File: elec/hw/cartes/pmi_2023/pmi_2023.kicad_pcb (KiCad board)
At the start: 2 copper layers, 85 x 73 mm, 183 parts, among them J1 USB4105-GF-A-060, J3 con_servo, Q1 2N7002E, SW5 2425755-1, U1 DRV8231ADDAR, U10 AD8531ARTZ, U11 GP2S60B, U12 GP2S60B, U13 GP2S60B, U14 GP2S60B, U15 GP2S60B, U16 GP2S60B, U17 GP2S60B, U18 GP2S60B, U19 tof_sensor_master, U2 SN74LVC1T45DBV, U20 tof_sensor_master, U21 tof_sensor_master, U22 tof_sensor_master, U23 tof_sensor_master, U24 tof_sensor_master, U25 tof_sensor_master, U26 tof_sensor_master, U27 KTS1622EUAA-TR, U28 PCA9685PW, U29 SN74LVC1T45DBV, U3 SN74LVC1T45DBV, U30 SN74LVC1T45DBV, U31 SN74LVC1T45DBV, U32 SN74LVC1T45DBV, U4 DRV8231ADDAR, U5 SN74LVC1T45DBV, U6 SN74LVC1T45DBV, U7 SN74LVC1T45DBV, U8 ESP32-S3-WROOM-1

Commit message: wip
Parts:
- removed C47: 1µF 16V, cocotter_capacitors:C_0805_2012Metric
- removed C48: 10µF 16V, cocotter_capacitors:C_0805_2012Metric
- removed D1: 1SS367,H3F, Diode_SMD:D_SOD-323
- removed D2: green, 0603, cocotter_diodes:LED_0603_1608Metric
- removed D3: yellow, 0603, cocotter_diodes:LED_0603_1608Metric
- removed R10, R11, R9: 0R, cocotter_resistor:r0603_reflow
- removed R12: 100k, cocotter_resistor:r0603_reflow
- removed SERVO0, SERVO1, SERVO2, SERVO3: con_servo, cocotter_connectors:ana_servo_5V
- added BATT_LOW1: red, 0603, cocotter_diodes:LED_0603_1608Metric, F.Cu at (183.8, 109.8)
- added BATT_OK1: red, 0603, cocotter_diodes:LED_0603_1608Metric, F.Cu at (183.8, 116.7)
- added BATT_WARN1: yellow, 0805, cocotter_diodes:LED_0805_2012Metric, F.Cu at (183.5, 113.2)
- added D7: red, 0603, cocotter_diodes:LED_0603_1608Metric, F.Cu at (103.8, 119.2)
- added F1: fuse_holder_5x20mm_TH, cocotter_connectors:PTF-15, F.Cu at (115.3, 104.7)
- added J2: con_servo, cocotter_connectors:ana_servo_5V, F.Cu at (269.4, 51.4)
- added J5: 254, cocotter_connectors:MY-18650-02, F.Cu at (170.6, 91.0)
- added J6: ~, cocotter_connectors:TTL-232R-3V3, F.Cu at (164.0, -77.8)
- added J7: USB4105-GF-A-060, cocotter_connectors:USB4105, F.Cu at (105.5, -81.1)
- added J8: 254, cocotter_connectors:MY-18650-02, F.Cu at (114.4, 91.0)
- added L1: 2.2µH, cocotter_inductors:L_Kyocera_07A7_7.3x6.6mm, F.Cu at (139.0, 20.5)
- added L2: 2.2µH, cocotter_inductors:L_Kyocera_07A7_7.3x6.6mm, F.Cu at (172.5, 103.5)
- added L3: 2.2µH, cocotter_inductors:L_Kyocera_07A7_7.3x6.6mm, F.Cu at (110.5, 113.5)
- added L4: 2.2µH, cocotter_inductors:L_Kyocera_07A7_7.3x6.6mm, F.Cu at (160.8, 103.5)
- added Q2: 2N7002, Package_TO_SOT_SMD:SOT-23, F.Cu at (94.5, -74.8)
- added Q3: DMP2008UFG-7, cocotter_transistors:Diodes_PowerDI3333-8, F.Cu at (118.2, 111.8)
- added R101: 0R, cocotter_resistor:r0603_reflow, F.Cu at (138.1, -45.4)
- added R102: 0R, cocotter_resistor:r0603_reflow, F.Cu at (151.1, -42.9)
- added R103: 0R, cocotter_resistor:r0603_reflow, F.Cu at (111.0, 104.7)
- added R104: 0R, cocotter_resistor:r0603_reflow, F.Cu at (114.0, 104.7)
- added R105: 0R, cocotter_resistor:r0603_reflow, F.Cu at (117.0, 104.7)
- added R106: 0R, cocotter_resistor:r0603_reflow, F.Cu at (119.5, 104.7)
- added R107: 10k, cocotter_resistor:r0603_reflow, F.Cu at (142.5, 29.0)
- added R108: 10k, cocotter_resistor:r0603_reflow, F.Cu at (176.0, 112.0)
- added R109: 100k, cocotter_resistor:r0603_reflow, F.Cu at (245.0, 97.0)
- added R110: 90k, cocotter_resistor:r0603_reflow, F.Cu at (113.0, 119.8)
- added R111: 10k, cocotter_resistor:r0603_reflow, F.Cu at (114.0, 122.0)
- added R112: 90k, cocotter_resistor:r0603_reflow, F.Cu at (164.0, 109.2)
- added R113: 10k, cocotter_resistor:r0603_reflow, F.Cu at (163.2, 111.5)
- added R114: 1k 1%, cocotter_resistor:r0603_reflow, F.Cu at (106.5, 118.5)
- added R13: 1k 1%, cocotter_resistor:r0603_reflow, F.Cu at (167.2, 129.8)
- added R20: 1k 1%, cocotter_resistor:r0603_reflow, F.Cu at (127.5, 132.5)
- added R21: 1k 1%, cocotter_resistor:r0603_reflow, F.Cu at (130.2, 134.0)
- added R22: 1k 1%, cocotter_resistor:r0603_reflow, F.Cu at (157.5, 134.0)
- added R25: 1k 1%, cocotter_resistor:r0603_reflow, F.Cu at (157.5, 132.5)
- added R26: 1k 1%, cocotter_resistor:r0603_reflow, F.Cu at (127.5, 135.5)
- added R57: 0R, cocotter_resistor:r0603_reflow, F.Cu at (168.0, 122.2)
- added R58: 0R, cocotter_resistor:r0603_reflow, F.Cu at (168.0, 119.2)
- added R59: 0R, cocotter_resistor:r0603_reflow, F.Cu at (171.2, 122.0)
- added R60: 0R, cocotter_resistor:r0603_reflow, F.Cu at (172.8, 122.0)
- added R61: 0R, cocotter_resistor:r0603_reflow, F.Cu at (168.0, 117.8)
- added R62: 1k 1%, cocotter_resistor:r0603_reflow, F.Cu at (182.2, 116.5)
- added R63: 1k 1%, cocotter_resistor:r0603_reflow, F.Cu at (181.8, 113.0)
- added SW6: 2425755-1, cocotter_connectors:2425755-1, F.Cu at (123.7, -49.4)
- added SW7: MSS12C02LS-BB2.0, cocotter_connectors:MSS12C02LS-BB2.0, F.Cu at (95.2, -78.0)
- added SW8: MSS12C02LS-BB2.0, cocotter_connectors:MSS12C02LS-BB2.0, F.Cu at (104.2, 114.0)
- added TP1: TestPoint, cocotter_others:testpoint-THT-0.5mm, F.Cu at (123.5, 114.5)
- added TP2: TestPoint, cocotter_others:testpoint-THT-0.5mm, F.Cu at (123.5, 116.2)
- added TP3: TestPoint, cocotter_others:testpoint-THT-0.5mm, F.Cu at (146.0, 140.5)
- added TP4: TestPoint, cocotter_others:testpoint-THT-0.5mm, F.Cu at (146.0, 142.0)
- added TP5: TestPoint, cocotter_others:testpoint-THT-0.5mm, F.Cu at (139.0, 139.0)
- added TP6: TestPoint, cocotter_others:testpoint-THT-0.5mm, F.Cu at (139.0, 137.5)
- added TP7: TestPoint, cocotter_others:testpoint-THT-0.5mm, F.Cu at (135.9, -48.2)
- added TP8: TestPoint, cocotter_others:testpoint-THT-0.5mm, F.Cu at (180.5, 123.5)
- added U34: TLV61070A, cocotter_ic:SOT-23-6, F.Cu at (161.0, 109.0)
- added U35: LDL1117S33R, cocotter_ic:SOT-223, F.Cu at (150.0, 23.2)
- C10, C31, C9: moved to B.Cu
- C11: value 22µF 16V -> 10µF 25V; footprint cocotter_capacitors:C_1206_3216Metric -> cocotter_capacitors:C_0805_2012Metric; moved to B.Cu
- C12, C3, C4: value 22µF 16V -> 100nF 50V; footprint cocotter_capacitors:C_1206_3216Metric -> cocotter_capacitors:C_0603_1608Metric
- C14, C23, C24, C26, C35: value 100nF 50V -> 10µF 25V; footprint cocotter_capacitors:C_0603_1608Metric -> cocotter_capacitors:C_0805_2012Metric
- C20, C28: value 10µF 16V -> 100nF 50V; footprint cocotter_capacitors:C_0805_2012Metric -> cocotter_capacitors:C_0603_1608Metric
- C25, C46: value 10µF 16V -> 10µF 25V
- C27, C30, C39, C40: value 100nF 50V -> 10µF 16V; footprint cocotter_capacitors:C_0603_1608Metric -> cocotter_capacitors:C_0805_2012Metric
- C29, C37, C41: value 100nF 50V -> 18nF 50V
- C36, C38, C5, C6: value 100nF 50V -> 47µF 10V; footprint cocotter_capacitors:C_0603_1608Metric -> cocotter_capacitors:C_1206_3216Metric
- C42: value 10µF 16V -> 18nF 50V; footprint cocotter_capacitors:C_0805_2012Metric -> cocotter_capacitors:C_0603_1608Metric
- C43, C44: value 10µF 16V -> 47µF 10V; footprint cocotter_capacitors:C_0805_2012Metric -> cocotter_capacitors:C_1206_3216Metric
- C45: value 10µF 16V -> 1µF 50V
- D5: value green, 0603 -> red, 0603
- D6: value green, 0603 -> 1N5819WS; footprint cocotter_diodes:LED_0603_1608Metric -> cocotter_diodes:D_SOD-323F
- J1: value USB4105-GF-A-060 -> con_servo; footprint cocotter_connectors:USB4105 -> cocotter_connectors:ana_servo_5V
- J4: value ~ -> con_servo; footprint cocotter_connectors:1051 -> cocotter_connectors:ana_servo_5V
- Q1: value 2N7002E -> ~; footprint Package_TO_SOT_SMD:SOT-23 -> cocotter_transistors:SOT-23-3
- R14, R15, R19, R23, R24, R27, R28, R64, R82, R83, R97, R98, R99: value 100k -> 1k 1%
- R16, R17, R18: value 10k -> 1k 1%
- R29, R54, R55, R56, R8: value 100k -> 0R
- R3, R38, R4, R5: value 10k -> 100k
- R31: value 0R -> 100k; moved to B.Cu
- R32, R87, R88, R89, R90, R93: value 0R -> 100k
- R34, R35, R46: value 100k -> 150R 1%; footprint cocotter_resistor:r0603_reflow -> cocotter_resistor:r0805_reflow; moved to B.Cu
- R36: value 0R -> 27k 1%; moved to B.Cu
- R37, R42, R43, R52, R53: value 100k -> 27k 1%; moved to B.Cu
- R40, R41, R47, R50, R51: value 1k 1% -> 150R 1%; footprint cocotter_resistor:r0603_reflow -> cocotter_resistor:r0805_reflow; moved to B.Cu
- R48, R49: value 1k 1% -> 27k 1%; moved to B.Cu
- R6, R7: value 0R -> 3k3 1%
- R65, R75: value 150R 1% -> 0R; footprint cocotter_resistor:r0805_reflow -> cocotter_resistor:r0603_reflow; moved to F.Cu
- R66: value 27k 1% -> 68k 1%; moved to F.Cu
- R67: value 150R 1% -> 90k; footprint cocotter_resistor:r0805_reflow -> cocotter_resistor:r0603_reflow; moved to F.Cu
- R68, R70: value 27k 1% -> 100k
- R69, R71: value 150R 1% -> 100k; footprint cocotter_resistor:r0805_reflow -> cocotter_resistor:r0603_reflow
- R72, R74, R76, R78: value 27k 1% -> 100k; moved to F.Cu
- R73, R77, R79: value 150R 1% -> 100k; footprint cocotter_resistor:r0805_reflow -> cocotter_resistor:r0603_reflow; moved to F.Cu
- R80: value 27k 1% -> 1k 1%
- R81: value 100k -> 1k 1%; moved to B.Cu
- R91, R92: value 0R -> 1k 1%
- R94: value 0R -> 10k
- R96: value 1k 1% -> 100k
- SW5: value 2425755-1 -> DS1040-04RN; footprint cocotter_connectors:2425755-1 -> cocotter_connectors:DS1040-04RN
- U10: value AD8531ARTZ -> tof_sensor_master; footprint cocotter_ic:SOT23-5 -> cocotter_connectors:tof_sensor_male
- U11, U17, U18: value GP2S60B -> tof_sensor_master; footprint cocotter_ic:GP2S60 -> cocotter_connectors:tof_sensor_male; moved to F.Cu
- U12: value GP2S60B -> LSM6DSO32XTR; footprint cocotter_ic:GP2S60 -> cocotter_ic:LGA-14_3x2.5mm_P0.5mm_LayoutBorder3x4y; moved to F.Cu
- U19, U20: value tof_sensor_master -> GP2S60B; footprint cocotter_connectors:tof_sensor_male -> cocotter_ic:GP2S60; moved to B.Cu
- U2: value SN74LVC1T45DBV -> DRV8231ADDAR; footprint Package_TO_SOT_SMD:SOT-23-6 -> cocotter_ic:DDA0008B
- U23: value tof_sensor_master -> PCA9685PW; footprint cocotter_connectors:tof_sensor_male -> Package_SO:TSSOP-28_4.4x9.7mm_P0.65mm
- U24, U25, U26: value tof_sensor_master -> SN74LVC1T45DBV; footprint cocotter_connectors:tof_sensor_male -> Package_TO_SOT_SMD:SOT-23-6
- U27: value KTS1622EUAA-TR -> SN74LVC1T45DBV; footprint cocotter_ic:TQFN44-24 -> Package_TO_SOT_SMD:SOT-23-6
- U28: value PCA9685PW -> TLV61070A; footprint Package_SO:TSSOP-28_4.4x9.7mm_P0.65mm -> cocotter_ic:SOT-23-6
- U29: value SN74LVC1T45DBV -> TLV61070A; footprint Package_TO_SOT_SMD:SOT-23-6 -> cocotter_ic:SOT-23-6
- U3: value SN74LVC1T45DBV -> EESX1321; footprint Package_TO_SOT_SMD:SOT-23-6 -> cocotter_ic:EESX1321
- U30: value SN74LVC1T45DBV -> TCA9535PWR; footprint Package_TO_SOT_SMD:SOT-23-6 -> Package_SO:TSSOP-24_4.4x7.8mm_P0.65mm
- U31: value SN74LVC1T45DBV -> ~; footprint Package_TO_SOT_SMD:SOT-23-6 -> cocotter_ic:OLED_0.96inch
- U32: value SN74LVC1T45DBV -> ESP32-S3-WROOM-1; footprint Package_TO_SOT_SMD:SOT-23-6 -> cocotter_ic:ESP32-S3-WROOM-1
- U33: value ~ -> TLV61070A; footprint cocotter_ic:OLED_0.96inch -> cocotter_ic:SOT-23-6
- U4: value DRV8231ADDAR -> EESX1321; footprint cocotter_ic:DDA0008B -> cocotter_ic:EESX1321
- U5: value SN74LVC1T45DBV -> AD8531ARTZ; footprint Package_TO_SOT_SMD:SOT-23-6 -> cocotter_ic:SOT23-5; moved to B.Cu
- U6, U7: value SN74LVC1T45DBV -> tof_sensor_master; footprint Package_TO_SOT_SMD:SOT-23-6 -> cocotter_connectors:tof_sensor_male
- U8: value ESP32-S3-WROOM-1 -> GP2S60B; footprint cocotter_ic:ESP32-S3-WROOM-1 -> cocotter_ic:GP2S60; moved to B.Cu
- U9: value ~ -> GP2S60B; footprint cocotter_ic:LGA-14_3x2.5mm_P0.5mm_LayoutBorder3x4y -> cocotter_ic:GP2S60; moved to B.Cu
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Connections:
- C10 pad 1: +BATT -> +3.3V
- C11 pad 1: +BATT -> +3.3V
- C12 pad 1: +BATT -> +3.3V
- C13 pad 1: /propulsion/encoder_supply -> +3V3
- C14 pad 1: /propulsion/encoder_supply -> +3V3
- C15 pad 1: +3.3V -> +3V3
- C16 pad 1: +3.3V -> +3V3
- C17 pad 1: +3.3V -> +3V3
- C18 pad 1: Net-(J3-5V) -> +3V3
- C19 pad 1: /com/EN_ESP32_3v3 -> +5V
- C2 pad 1: +BATT -> +3.3V
- C20 pad 1: +3.3V -> +5V
- C21 pad 1: +3.3V -> +5V
- C22 pad 1: /com/esp32_vbatt_mon_2v9 -> +5V
- C23 pad 1: +3.3V -> +5V
- C24 pad 1: Net-(U10-+) -> +5V
- C25 pad 1: +3.3V -> +5V
- C26 pad 1: +3.3V -> +5V
- C27 pad 1: +3V3 -> +BATT
- C29 pad 1: +3V3 -> /power_supply/P3V9
- C29 pad 2: GND -> Net-(U28-FB)
- C3 pad 1: +BATT -> /propulsion/Vmot_left_5V
- C30 pad 1: +5V -> +BATT
- C31 pad 1: +3V3 -> +3.3V
- C32 pad 1: +5V -> /com/EN_ESP32_3v3
- C33 pad 1: +3V3 -> /com/esp32_vbatt_mon_2v9
- C34 pad 1: +5V -> +3.3V
- C35 pad 1: +3V3 -> +3.3V
- C36 pad 1: +5V -> /power_supply/P3V9
- C37 pad 1: +3V3 -> +5V
- C37 pad 2: GND -> Net-(U29-FB)
- C39 pad 1: +3.3V -> +BATT
- C4 pad 1: +BATT -> /propulsion/Vmot_right_5V
- C40 pad 1: /propulsion/encoder_supply -> +BATT
- C41 pad 1: /propulsion/encoder_supply -> /power_supply/Vmot_left_5V
- C41 pad 2: GND -> Net-(U33-FB)
- C42 pad 1: +5V -> /power_supply/Vmot_right_5V
- C42 pad 2: GND -> Net-(U34-FB)
- C43 pad 1: Net-(J3-5V) -> /power_supply/Vmot_left_5V
- C44 pad 1: +5V -> /power_supply/Vmot_right_5V
- C45 pad 1: +5V -> /power_supply/P3V9
- C46 pad 1: +5V -> +3.3V
- C5 pad 1: +3.3V -> /propulsion/Vmot_left_5V
- C6 pad 1: /propulsion/encoder_supply -> /propulsion/Vmot_right_5V
- C8 pad 1: +3.3V -> /propulsion/encoder_supply
- C9 pad 1: +3.3V -> Net-(U5-+)
- D4 pad A: (no net) -> Net-(D4-PadA)
- D4 pad C: (no net) -> GND
- D5 pad A: (no net) -> Net-(D5-PadA)
- D5 pad C: (no net) -> GND
- J3 pad 2: Net-(J3-5V) -> +5V
- J3 pad 3: /propulsion/pwm_vaccum_5v -> /actuators/servo_pwm_2_5V
- Q1 pad 1: /com/USB_VBUS -> /propulsion/pwm_vaccum_3v3
- R1 pad 1: /propulsion/pwm_left -> /propulsion/dir_left
- R100 pad 1: +3.3V -> Net-(R100-Pad1)
- R100 pad 2: /interface/esp32_sda_3v3 -> /com/scl_3v3
- R14 pad 1: /propulsion/dir_right -> Net-(U3-C2)
- R15 pad 1: /propulsion/pwm_right -> Net-(U4-C1)
- R16 pad 1: /com/i_prop_right_3v3 -> Net-(U4-C2)
- R17 pad 1: /com/i_prop_right_3v3 -> Net-(U3-E2)
- R17 pad 2: GND -> /propulsion/right_encod_B_3v3
- R18 pad 1: /com/i_prop_right_3v3 -> /propulsion/right_encod_B_3v3
- R19 pad 1: +3.3V -> Net-(U3-E2)
- R19 pad 2: /propulsion/nREAD_encoder_3v3 -> /propulsion/right_encod_B_3v3
- R2 pad 1: /propulsion/dir_left -> /propulsion/dir_right
- R23 pad 1: /propulsion/right_encod_A_5V -> /propulsion/right_encod_A_3v3
- R24 pad 1: /propulsion/right_encod_B_5V -> Net-(U4-E2)
- R24 pad 2: GND -> /propulsion/left_encod_B_3v3
- R27 pad 1: +3.3V -> /propulsion/left_encod_A_3v3
- R27 pad 2: /com/EN_ESP32_3v3 -> GND
- R28 pad 1: Net-(U8-IO46,GPIO46) -> Net-(U4-E1)
- R28 pad 2: GND -> /propulsion/left_encod_A_3v3
- R29 pad 1: /propulsion/pwm_vaccum_3v3 -> /propulsion/encoder_supply
- R29 pad 2: GND -> +5V
- R3 pad 1: /com/i_prop_left_3v3 -> /propulsion/pwm_left
- R30 pad 1: Net-(U7-DIR) -> /propulsion/encoder_supply
- R31 pad 1: Net-(J3-5V) -> /actuators/line_led_pwm_3v3
- R31 pad 2: +5V -> Net-(U5-+)
- R32 pad 1: Net-(J3-5V) -> +3.3V
- R32 pad 2: +3.3V -> /sensors/ctc_left
- R33 pad 2: Net-(U8-IO45,GPIO45) -> /sensors/ctc_rigth
- R34 pad 1: Net-(U8-IO45,GPIO45) -> /sensors/line_led_3v3
- R34 pad 2: GND -> Net-(U8-A)
- R35 pad 1: +3V3 -> /sensors/line_led_3v3
- R35 pad 2: /com/i2C_io_int_3v3 -> Net-(U9-A)
- R36 pad 1: Net-(U27-ADDR) -> +3.3V
- R36 pad 2: GND -> /line_detect_l0
- R37 pad 1: +3V3 -> +3.3V
- R37 pad 2: Net-(U27-nRESET) -> /line_detect_r0
- R38 pad 1: /com/boot/dl_select_3v3 -> +3.3V
- R38 pad 2: Net-(R38-Pad2) -> Net-(U12-INT2/DEN)
- R39 pad 2: /com/boot/dl_select_3v3 -> /com/gyro_ncs_3v3
- R4 pad 1: /com/i_prop_left_3v3 -> /propulsion/pwm_right
- R40 pad 1: Net-(U8-TXD0,U0TXD,GPIO43,CLK_OUT1) -> /sensors/line_led_3v3
- R40 pad 2: /com/esp32_dbg_tx_3v3 -> Net-(U13-A)
- R41 pad 1: Net-(U8-TXD0,U0TXD,GPIO43,CLK_OUT1) -> /sensors/line_led_3v3
- R41 pad 2: /com/esp32_dbg_tx_3v3 -> Net-(U14-A)
- R42 pad 1: /interface/conf0 -> +3.3V
- R42 pad 2: GND -> /line_detect_l1
- R43 pad 2: /com/esp32_dbg_rx_3v3 -> /line_detect_r1
- R44 pad 1: Net-(R44-Pad1) -> +3.3V
- R44 pad 2: /com/vbatt_mon_8.7V -> Net-(U12-SCx)
- R45 pad 1: /com/esp32_vbatt_mon_2v9 -> +3.3V
- R45 pad 2: Net-(R44-Pad1) -> Net-(U12-SDx)
- R46 pad 1: GND -> /sensors/line_led_3v3
- R46 pad 2: /com/esp32_vbatt_mon_2v9 -> Net-(U15-A)
- R47 pad 1: /com/led_esp_3v3 -> /sensors/line_led_3v3
- R47 pad 2: Net-(D5-A) -> Net-(U16-A)
- R48 pad 1: /com/led_com_3v3 -> +3.3V
- R48 pad 2: Net-(D6-A) -> /line_detect_l2
- R49 pad 1: +3V3 -> +3.3V
- R49 pad 2: Net-(D2-A) -> /line_detect_r2
- R5 pad 1: /com/i_prop_left_3v3 -> /propulsion/pwm_vaccum_3v3
- R50 pad 1: +3V3 -> /sensors/line_led_3v3
- R50 pad 2: Net-(D3-A) -> Net-(U19-A)
- R51 pad 1: +3V3 -> /sensors/line_led_3v3
- R51 pad 2: Net-(D4-A) -> Net-(U20-A)
- R52 pad 1: /com/USB_VBUS -> +3.3V
- R52 pad 2: GND -> /line_detect_l3
- R53 pad 2: Net-(U9-SCx) -> /line_detect_r3
- R54 pad 1: +3.3V -> Net-(U23-EXTCLK)
- R54 pad 2: Net-(U9-SDx) -> GND
- R55 pad 1: +3.3V -> /actuators/servos_nOE
- R55 pad 2: /com/gyro_ncs_3v3 -> GND
- R56 pad 1: +3.3V -> Net-(U23-A1)
- R56 pad 2: Net-(U9-INT1) -> GND
- R6 pad 1: +5V -> /com/i_prop_right_3v3
- R6 pad 2: /propulsion/encoder_supply -> GND
- R64 pad 1: /actuators/line_led_pwm_3v3 -> +3V3
- R64 pad 2: Net-(U10-+) -> Net-(BATT_LOW1-PadA)
- R65 pad 1: /sensors/line_led_3v3 -> +BATT
- R65 pad 2: Net-(U11-A) -> /com/vbatt_mon_4.35V
- R66 pad 1: +3.3V -> /power_supply/P3V9
- R66 pad 2: /line_detect_l0 -> Net-(U28-FB)
- R67 pad 1: /sensors/line_led_3v3 -> +5V
- R67 pad 2: Net-(U12-A) -> Net-(U29-FB)
- R68 pad 1: +3.3V -> /interface/conf0
- R68 pad 2: /line_detect_l1 -> GND
- R69 pad 1: /sensors/line_led_3v3 -> /interface/conf1
- R69 pad 2: Net-(U13-A) -> GND
- R7 pad 1: +3.3V -> /com/i_prop_left_3v3
- R7 pad 2: /propulsion/encoder_supply -> GND
- R70 pad 1: +3.3V -> /interface/conf2
- R70 pad 2: /line_detect_l2 -> GND
- R71 pad 1: /sensors/line_led_3v3 -> /interface/conf3
- R71 pad 2: Net-(U14-A) -> GND
- R72 pad 1: +3.3V -> /interface/select2
- R72 pad 2: /line_detect_l3 -> GND
- R73 pad 1: /sensors/line_led_3v3 -> /interface/select1
- R73 pad 2: Net-(U15-A) -> GND
- R74 pad 1: +3.3V -> +3V3
- R74 pad 2: /line_detect_r0 -> /com/i2C_io_int_3v3
- R75 pad 1: /sensors/line_led_3v3 -> Net-(U30-A2)
- R75 pad 2: Net-(U16-A) -> GND
- R76 pad 1: +3.3V -> +3V3
- R76 pad 2: /line_detect_r1 -> /interface/u30_unused_p17
- R77 pad 1: /sensors/line_led_3v3 -> /interface/select4
- R77 pad 2: Net-(U17-A) -> GND
- R78 pad 1: +3.3V -> /interface/select3
- R78 pad 2: /line_detect_r2 -> GND
- R79 pad 1: /sensors/line_led_3v3 -> /interface/select0
- R79 pad 2: Net-(U18-A) -> GND
- R8 pad 1: /propulsion/left_encod_A_5V -> Net-(R8-Pad1)
- R8 pad 2: GND -> /propulsion/Vmot_left_5V
- R80 pad 2: /line_detect_r3 -> /interface/esp32_scl_3v3
- R81 pad 2: /sensors/ctc_left -> /interface/esp32_sda_3v3
- R82 pad 1: +3.3V -> /com/led_esp_3v3
- R82 pad 2: /sensors/ctc_rigth -> Net-(D4-PadA)
- R83 pad 1: /interface/conf1 -> /com/led_com_3v3
- R83 pad 2: GND -> Net-(D5-PadA)
- R84 pad 1: /interface/conf2 -> GND
- R84 pad 2: GND -> /com/esp32_vbatt_mon_2v9
- R85 pad 1: /interface/conf3 -> /com/esp32_vbatt_mon_2v9
- R85 pad 2: GND -> /com/vbatt_mon_4.35V
- R86 pad 1: /interface/select2 -> +3.3V
- R86 pad 2: GND -> /com/EN_ESP32_3v3
- R87 pad 1: /actuators/servos_nOE -> /com/esp32_vbatt_mon_2v9
- R87 pad 2: GND -> /com/vbatt_mon_4.35V
- R88 pad 1: Net-(U28-EXTCLK) -> +3.3V
- R88 pad 2: GND -> Net-(U32-IO45,GPIO45)
- R89 pad 1: Net-(U28-A1) -> Net-(U32-IO45,GPIO45)
- R90 pad 1: Net-(U28-A2) -> Net-(U32-IO46,GPIO46)
- R91 pad 1: Net-(U28-A4) -> Net-(U32-TXD0,U0TXD,GPIO43,CLK_OUT1)
- R91 pad 2: GND -> /com/esp32_dbg_tx_3v3
- R92 pad 1: +3V3 -> Net-(U32-TXD0,U0TXD,GPIO43,CLK_OUT1)
- R92 pad 2: Net-(U28-A0) -> /com/esp32_dbg_tx_3v3
- R93 pad 1: +3V3 -> +3.3V
- R93 pad 2: Net-(U28-A3) -> /com/boot/dl_select_3v3
- R94 pad 1: +3V3 -> /com/boot/dl_select_3v3
- R94 pad 2: Net-(U28-A5) -> Net-(R94-Pad2)
- R95 pad 1: /interface/select1 -> +3.3V
- R95 pad 2: GND -> /com/esp32_dbg_rx_3v3
- R96 pad 1: +3.3V -> /com/USB_VBUS
- R96 pad 2: /interface/esp32_scl_3v3 -> GND
- R97 pad 1: /interface/select4 -> Net-(R97-Pad1)
- R97 pad 2: GND -> /com/sda_3v3
- R98 pad 1: /interface/select3 -> +3.3V
- R98 pad 2: GND -> Net-(R97-Pad1)
- R99 pad 1: /interface/select0 -> +3.3V
- R99 pad 2: GND -> Net-(R100-Pad1)
- SW5 pad 1: /interface/select0 -> /interface/conf0
- SW5 pad 2: /interface/select4 -> /interface/conf1
- SW5 pad 3: /interface/select3 -> /interface/conf2
- SW5 pad 4: /interface/select2 -> /interface/conf3
- SW5 pad 6: /interface/select1 -> +3.3V
- U1 pad 5: +BATT -> /propulsion/Vmot_left_5V
- U1 pad 6: Net-(ML1-M+) -> /propulsion/mot_left_A
- U1 pad 8: Net-(ML1-M-) -> /propulsion/mot_left_B
- U10 pad 1: /sensors/line_led_3v3 -> GND
- U10 pad 2: GND -> +3.3V
- U10 pad 3: Net-(U10-+) -> /sensors/enable_tof2
- U10 pad 4: /sensors/line_led_3v3 -> /sensors/tof_irq
- U10 pad 5: +3.3V -> /com/sda_3v3
- U11 pad 1: /line_detect_l0 -> GND
- U11 pad 2: GND -> +3.3V
- U11 pad 3: GND -> /sensors/enable_tof6
- U11 pad 4: Net-(U11-A) -> /sensors/tof_irq
- U12 pad 1: /line_detect_l1 -> /com/gyro_miso_3v3
- U12 pad 2: GND -> Net-(U12-SDx)
- U12 pad 3: GND -> Net-(U12-SCx)
- U12 pad 4: Net-(U12-A) -> Net-(U12-INT1)
- U13 pad 1: /line_detect_l2 -> /line_detect_l1
- U14 pad 1: /line_detect_l3 -> /line_detect_r1
- U15 pad 1: /line_detect_r0 -> /line_detect_l2
- U16 pad 1: /line_detect_r1 -> /line_detect_r2
- U17 pad 1: /line_detect_r2 -> GND
- U17 pad 2: GND -> +3.3V
- U17 pad 3: GND -> /sensors/enable_tof3
- U17 pad 4: Net-(U17-A) -> /sensors/tof_irq
- U18 pad 1: /line_detect_r3 -> GND
- U18 pad 2: GND -> +3.3V
- U18 pad 3: GND -> /sensors/enable_tof7
- U18 pad 4: Net-(U18-A) -> /sensors/tof_irq
- U19 pad 1: GND -> /line_detect_l3
- U19 pad 2: +3.3V -> GND
- U19 pad 3: /sensors/enable_tof1 -> GND
- U19 pad 4: /sensors/tof_irq -> Net-(U19-A)
- U2 pad 1: +3.3V -> /com/i_prop_right_3v3
- U2 pad 2: GND -> /propulsion/dir_right
- U2 pad 3: /propulsion/left_encod_A_3v3 -> /propulsion/pwm_right
- U2 pad 4: /propulsion/left_encod_A_5V -> +3.3V
- U2 pad 5: /propulsion/nREAD_encoder_3v3 -> /propulsion/Vmot_right_5V
- U2 pad 6: /propulsion/encoder_supply -> /propulsion/mot_right_A
- U20 pad 1: GND -> /line_detect_r3
- U20 pad 2: +3.3V -> GND
- U20 pad 3: /sensors/enable_tof2 -> GND
- U20 pad 4: /sensors/tof_irq -> Net-(U20-A)
- U21 pad 3: /sensors/enable_tof3 -> /sensors/enable_tof4
- U21 pad 7: /sensors/enable_tof2 -> /sensors/enable_tof3
- U22 pad 3: /sensors/enable_tof4 -> unconnected-(U22-enable_next_board_3v3-Pad3)
- U22 pad 7: /sensors/enable_tof3 -> /sensors/enable_tof7
- U23 pad 1: GND -> Net-(U23-A0)
- U23 pad 2: +3.3V -> Net-(U23-A1)
- U23 pad 3: /sensors/enable_tof5 -> Net-(U23-A2)
- U23 pad 4: /sensors/tof_irq -> Net-(U23-A3)
- U23 pad 5: /com/sda_3v3 -> Net-(U23-A4)
- U23 pad 6: /com/scl_3v3 -> /actuators/servo_pwm_0_3v3
- U23 pad 7: /sensors/enable_tof4 -> /actuators/servo_pwm_1_3v3
- U23 pad 8: /actuators//reset_tof_3v3 -> /actuators/servo_pwm_2_3v3
- U24 pad 1: GND -> +3V3
- U24 pad 2: +3.3V -> GND
- U24 pad 3: /sensors/enable_tof6 -> /actuators/servo_pwm_0_3v3
- U24 pad 4: /sensors/tof_irq -> /actuators/servo_pwm_0_5V
- U24 pad 5: /com/sda_3v3 -> +3V3
- U24 pad 6: /com/scl_3v3 -> +5V
- U25 pad 1: GND -> +3V3
- U25 pad 2: +3.3V -> GND
- U25 pad 3: /sensors/enable_tof7 -> /actuators/servo_pwm_1_3v3
- U25 pad 4: /sensors/tof_irq -> /actuators/servo_pwm_1_5V
- U25 pad 5: /com/sda_3v3 -> +3V3
- U25 pad 6: /com/scl_3v3 -> +5V
- U26 pad 1: GND -> +3V3
- U26 pad 2: +3.3V -> GND
- U26 pad 3: unconnected-(U26-enable_next_board_3v3-Pad3) -> /actuators/servo_pwm_2_3v3
- U26 pad 4: /sensors/tof_irq -> /actuators/servo_pwm_2_5V
- U26 pad 5: /com/sda_3v3 -> +3V3
- U26 pad 6: /com/scl_3v3 -> +5V
- U27 pad 1: /interface/conf0 -> +3V3
- U27 pad 2: /interface/conf1 -> GND
- U27 pad 3: /interface/conf2 -> /actuators/servo_pwm_3_3v3
- U27 pad 4: /interface/conf3 -> /actuators/servo_pwm_3_5V
- U27 pad 5: /interface/select0 -> +3V3
- U27 pad 6: /interface/select1 -> +5V
- U28 pad 1: Net-(U28-A0) -> Net-(U28-SW)
- U28 pad 2: Net-(U28-A1) -> GND
- U28 pad 3: Net-(U28-A2) -> /power_supply/enable_pw_conv_3v7
- U28 pad 4: Net-(U28-A3) -> Net-(U28-FB)
- U28 pad 5: Net-(U28-A4) -> /power_supply/P3V9
- U28 pad 6: /actuators/servo_pwm_0_3v3 -> +BATT
- U29 pad 1: +3V3 -> Net-(U29-SW)
- U29 pad 3: /actuators/servo_pwm_0_3v3 -> /power_supply/enable_pw_conv_3v7
- U29 pad 4: /actuators/servo_pwm_0_5V -> Net-(U29-FB)
- U29 pad 5: +3V3 -> +5V
- U29 pad 6: +5V -> +BATT
- U3 pad 2: GND -> Net-(U3-C1)
- U3 pad 3: /propulsion/left_encod_B_3v3 -> Net-(U3-C2)
- U3 pad 4: /propulsion/left_encod_B_5V -> Net-(U3-E1)
- U3 pad 5: /propulsion/nREAD_encoder_3v3 -> Net-(U3-E2)
- U30 pad 1: +3V3 -> /com/i2C_io_int_3v3
- U30 pad 2: GND -> Net-(U30-A1)
- U30 pad 3: /actuators/servo_pwm_1_3v3 -> Net-(U30-A2)
- U30 pad 4: /actuators/servo_pwm_1_5V -> /interface/conf0
- U30 pad 5: +3V3 -> /interface/conf1
- U30 pad 6: +5V -> /interface/conf2
- U31 pad 1: +3V3 -> GND
- U31 pad 2: GND -> +3.3V
- U31 pad 3: /actuators/servo_pwm_2_3v3 -> /interface/esp32_scl_3v3
- U31 pad 4: /actuators/servo_pwm_2_5V -> /interface/esp32_sda_3v3
- U32 pad 1: +3V3 -> GND
- U32 pad 2: GND -> +3.3V
- U32 pad 3: /actuators/servo_pwm_3_3v3 -> /com/EN_ESP32_3v3
- U32 pad 4: /actuators/servo_pwm_3_5V -> /com/led_esp_3v3
- U32 pad 5: +3V3 -> /com/led_com_3v3
- U32 pad 6: +5V -> /propulsion/pwm_left
- U33 pad 1: (no net) -> Net-(U33-SW)
- U33 pad 2: +3.3V -> GND
- U33 pad 3: /interface/esp32_scl_3v3 -> /power_supply/enable_pw_conv_3v7
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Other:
- outline, holes or cut-outs redrawn
- board text added: "+"
- board text added: "-"
- board text added: "10A"

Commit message: wip
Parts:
- removed C28: 100nF 50V, cocotter_capacitors:C_0603_1608Metric
- removed R101, R102: 0R, cocotter_resistor:r0603_reflow
- removed TP7: TestPoint, cocotter_others:testpoint-THT-0.5mm
- removed U18, U22: tof_sensor_master, cocotter_connectors:tof_sensor_male
- removed U30: TCA9535PWR, Package_SO:TSSOP-24_4.4x7.8mm_P0.65mm
- added C47: 100nF 50V, cocotter_capacitors:C_0603_1608Metric, F.Cu at (146.3, 50.5)
- added C48: 10µF 25V, cocotter_capacitors:C_0805_2012Metric, F.Cu at (146.5, 47.8)
- added C49: 10µF 25V, cocotter_capacitors:C_0805_2012Metric, F.Cu at (181.5, -48.8)
- added C50: 100nF 50V, cocotter_capacitors:C_0603_1608Metric, F.Cu at (181.3, -46.0)
- added D1: ~, cocotter_diodes:3528_PLCC-Reverse_mount, F.Cu at (142.5, 83.0)
- added F2: 10A F, cocotter_others:JFC2410, F.Cu at (136.8, 98.0)
- added F3: 10A F, cocotter_others:JFC2410, F.Cu at (148.2, 98.0)
- added H1: MountingHole, MountingHole:MountingHole_2.1mm, F.Cu at (121.2, 120.8)
- added H2: MountingHole, MountingHole:MountingHole_2.1mm, F.Cu at (121.2, 146.0)
- added H3: MountingHole, MountingHole:MountingHole_2.1mm, F.Cu at (163.8, 121.0)
- added H4: MountingHole, MountingHole:MountingHole_2.1mm, F.Cu at (164.0, 146.0)
- added R10: 0R, cocotter_resistor:r0603_reflow, F.Cu at (142.5, 49.9)
- added R11: 0R, cocotter_resistor:r0603_reflow, F.Cu at (142.5, 52.4)
- added R115: 100k, cocotter_resistor:r0603_reflow, F.Cu at (177.4, -55.0)
- added R116: 0R, cocotter_resistor:r0603_reflow, F.Cu at (177.4, -52.5)
- added R117: 0R, cocotter_resistor:r0603_reflow, F.Cu at (177.4, -50.1)
- added R118: 0R, cocotter_resistor:r0603_reflow, F.Cu at (177.4, -47.6)
- added R12: 0R, cocotter_resistor:r0603_reflow, F.Cu at (142.5, 54.8)
- added R9: 100k, cocotter_resistor:r0603_reflow, F.Cu at (142.5, 47.5)
- added SW1: ESE22MH22, cocotter_connectors:ESE22MH22, F.Cu at (170.8, 151.2)
- added SW2: ESE22MH24, cocotter_connectors:ESE22MH24, F.Cu at (114.2, 151.3)
- F1: value fuse_holder_5x20mm_TH -> 10A F; footprint cocotter_connectors:PTF-15 -> cocotter_others:JFC2410
- R74: value 100k -> 330R 1%
- R75: value 0R -> 51R 1%
- R76: value 100k -> 51R 1%
- U11, U7: value tof_sensor_master -> XRA1200PIG16TR-F; footprint cocotter_connectors:tof_sensor_male -> cocotter_ic:TSSOP-16_4.4x5mm_P0.65mm
- U5: footprint cocotter_ic:SOT23-5 -> cocotter_ic:SOT-23-5
- moved R33 248.1 mm to (116.5, -66.2)
- moved R32 232.5 mm to (116.8, -69.8)
- moved D4 217.1 mm to (92.8, -99.0)
- moved D5 217.1 mm to (92.8, -103.5)
- moved R82 217.1 mm to (89.3, -99.0)
- moved R83 217.1 mm to (89.3, -103.5)
- moved C12 184.7 mm to (112.5, -25.1)
- moved R109 184.7 mm to (107.5, -26.3)
- moved R38 184.7 mm to (116.0, -27.3)
- moved R39 184.7 mm to (112.8, -31.1)
- moved R44 184.7 mm to (107.5, -27.8)
- moved R45 184.7 mm to (107.5, -29.3)
- moved U12 184.7 mm to (112.2, -27.6)
- moved U25 167.6 mm to (128.5, 150.5)
- moved J2 167.0 mm to (135.0, 150.5), turned to -90 degrees
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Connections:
- F1 pad 1: +BATT -> Net-(F1-Pad1)
- F1 pad 2: Net-(F1-Pad2) -> +BATT
- Q3 pad 1: Net-(F1-Pad2) -> Net-(F1-Pad1)
- Q3 pad 2: Net-(F1-Pad2) -> Net-(F1-Pad1)
- Q3 pad 3: Net-(F1-Pad2) -> Net-(F1-Pad1)
- R103 pad 1: Net-(F1-Pad2) -> Net-(F1-Pad1)
- R104 pad 1: Net-(F1-Pad2) -> Net-(F1-Pad1)
- R105 pad 1: Net-(F1-Pad2) -> Net-(F1-Pad1)
- R106 pad 1: Net-(F1-Pad2) -> Net-(F1-Pad1)
- R74 pad 1: +3V3 -> /actuators/LED_RGB_R_3v3
- R74 pad 2: /com/i2C_io_int_3v3 -> Net-(D1-C_RED)
- R75 pad 1: Net-(U30-A2) -> /actuators/LED_RGB_G_3v3
- R75 pad 2: GND -> Net-(D1-C_GREEN)
- R76 pad 1: +3V3 -> /actuators/LED_RGB_B_3v3
- R76 pad 2: /interface/u30_unused_p17 -> Net-(D1-C_BLUE)
- U11 pad 1: GND -> Net-(U11-A0)
- U11 pad 2: +3.3V -> Net-(U11-A1)
- U11 pad 3: /sensors/enable_tof6 -> Net-(U11-A2)
- U11 pad 4: /sensors/tof_irq -> /interface/conf0
- U11 pad 5: /com/sda_3v3 -> /interface/conf1
- U11 pad 6: /com/scl_3v3 -> /interface/conf2
- U11 pad 7: /sensors/enable_tof5 -> /interface/conf3
- U11 pad 8: /actuators//reset_tof_3v3 -> GND
- U21 pad 3: /sensors/enable_tof4 -> unconnected-(U21-enable_next_board_3v3-Pad3)
- U7 pad 1: GND -> Net-(U7-A0)
- U7 pad 2: +3.3V -> Net-(U7-A1)
- U7 pad 3: /sensors/enable_tof5 -> Net-(U7-A2)
- U7 pad 4: /sensors/tof_irq -> /line_detect_l0
- U7 pad 5: /com/sda_3v3 -> /line_detect_l1
- U7 pad 6: /com/scl_3v3 -> /line_detect_l2
- U7 pad 7: /sensors/enable_tof4 -> /line_detect_l3
- U7 pad 8: /actuators//reset_tof_3v3 -> GND
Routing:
- net GND: track 0.00 -> 59.0 mm
- net /power_supply/P3V9: track 0.00 -> 14.2 mm
- net /power_supply/enable_pw_conv_3v7: track 0.00 -> 7.98 mm
- net Net-(U28-FB): track 0.00 -> 5.53 mm
- net Net-(U28-SW): track 0.00 -> 4.76 mm
- net Net-(U32-IO45,GPIO45): track 0.00 -> 4.47 mm
- net +3.3V: track 0.00 -> 4.32 mm
- net /sensors/line_led_3v3: track 0.00 -> 4.07 mm
- net Net-(U5-+): track 0.00 -> 3.37 mm
- net Net-(U20-A): track 0.00 -> 1.81 mm
- net Net-(U9-A): track 0.00 -> 1.54 mm
- net Net-(U8-A): track 0.00 -> 1.54 mm
- net Net-(U16-A): track 0.00 -> 1.54 mm
- net Net-(U15-A): track 0.00 -> 1.54 mm
- net Net-(U14-A): track 0.00 -> 1.54 mm
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- added copper zone on F.Cu, net +BATT
- added copper zone on F.Cu, net /power_supply/P3V9
- added copper zone on F.Cu, net Net-(U28-SW)
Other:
- outline, holes or cut-outs redrawn
- board text added: "C1"
- board text added: "locked"
- board text removed: "+"
- board text removed: "-"

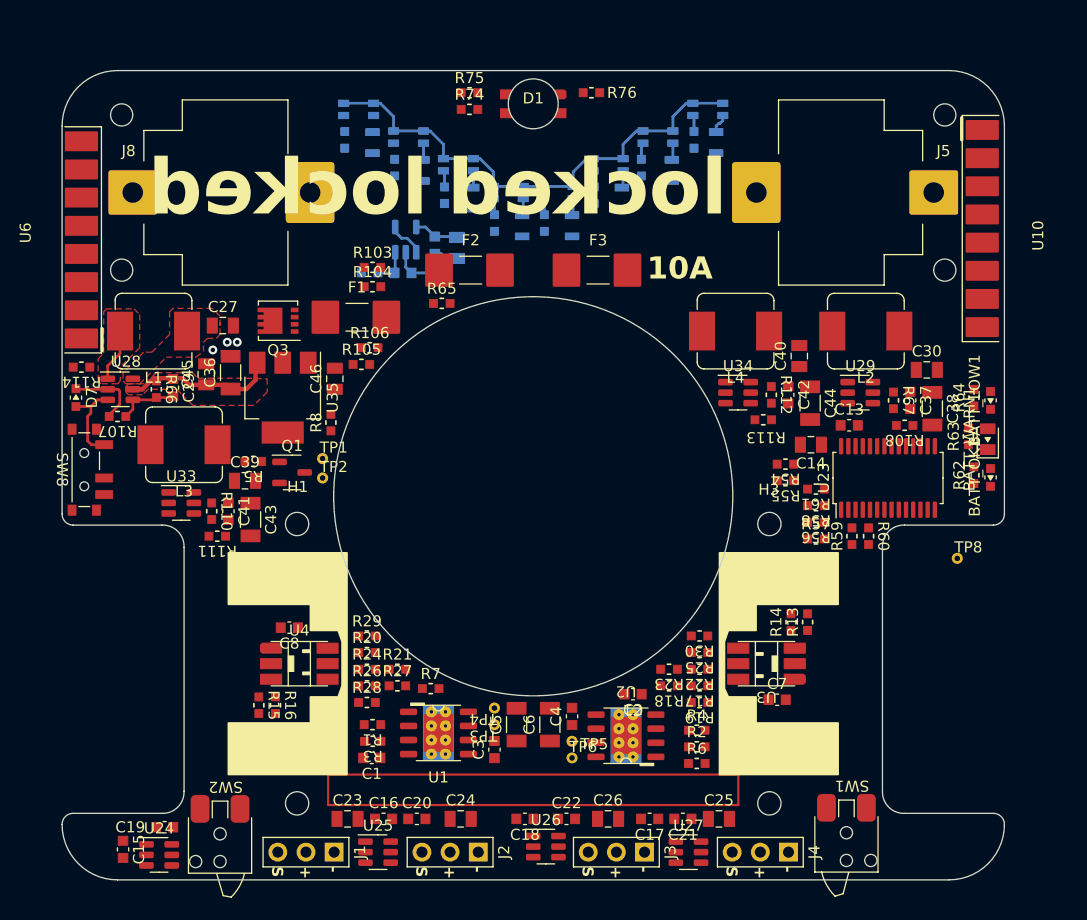
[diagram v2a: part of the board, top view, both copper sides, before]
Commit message: pmi layout (WIP)
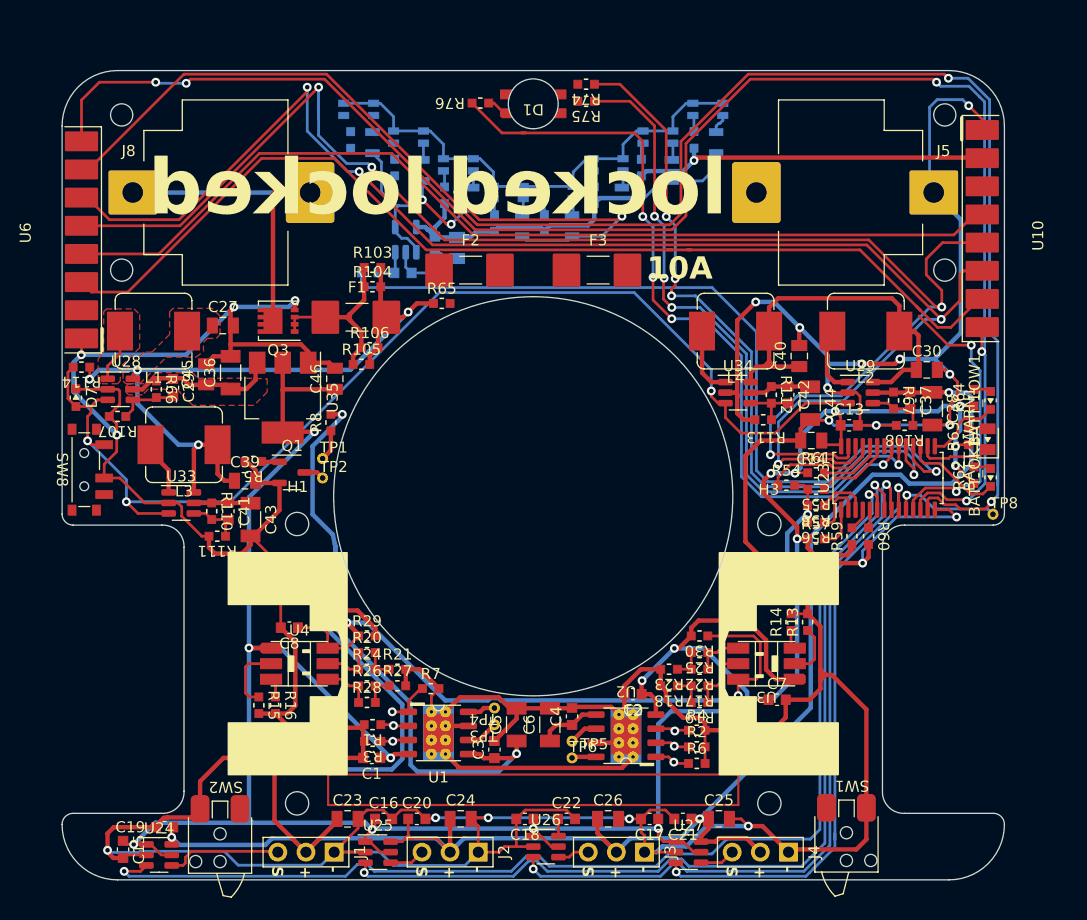
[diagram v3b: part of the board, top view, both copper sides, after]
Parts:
- moved R74 10.8 mm to (147.3, 81.2), turned to 180 degrees
- moved R75 10.5 mm to (147.3, 82.8), turned to 180 degrees
- moved R76 10.1 mm to (137.7, 82.9), turned to 0 degrees
- moved TP8 5.12 mm to (184.0, 120.0)
- moved R55 2.86 mm to (168.0, 117.8)
- moved R54 1.91 mm to (165.3, 117.4), turned to 0 degrees
- moved R61 1.47 mm to (168.0, 116.3), turned to 0 degrees
- moved R52 0.53 mm to (126.0, 86.3)
- moved C14 0.38 mm to (167.6, 113.4)
- turned D1 to 180 degrees
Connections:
- C1 pad 1: +3.3V -> +3V3
- C10 pad 1: +3.3V -> +3V3
- C11 pad 1: +3.3V -> +3V3
- C12 pad 1: +3.3V -> +3V3
- C2 pad 1: +3.3V -> +3V3
- C31 pad 1: +3.3V -> +3V3
- C34 pad 1: +3.3V -> +3V3
- C35 pad 1: +3.3V -> +3V3
- C46 pad 1: +3.3V -> +3V3
- C47 pad 1: +3.3V -> +3V3
- C48 pad 1: +3.3V -> +3V3
- C49 pad 1: +3.3V -> +3V3
- C50 pad 1: +3.3V -> +3V3
- D1 pad 4: +3.3V -> +3V3
- D6 pad 1: +3.3V -> +3V3
- R109 pad 1: +3.3V -> +3V3
- R115 pad 1: +3.3V -> +3V3
- R118 pad 1: +3.3V -> +3V3
- R30 pad 2: +3.3V -> +3V3
- R32 pad 1: +3.3V -> +3V3
- R33 pad 1: +3.3V -> +3V3
- R36 pad 1: +3.3V -> +3V3
- R37 pad 1: +3.3V -> +3V3
- R38 pad 1: +3.3V -> +3V3
- R39 pad 1: +3.3V -> +3V3
- R42 pad 1: +3.3V -> +3V3
- R43 pad 1: +3.3V -> +3V3
- R44 pad 1: +3.3V -> +3V3
- R45 pad 1: +3.3V -> +3V3
- R48 pad 1: +3.3V -> +3V3
- R49 pad 1: +3.3V -> +3V3
- R52 pad 1: +3.3V -> +3V3
- R53 pad 1: +3.3V -> +3V3
- R80 pad 1: +3.3V -> +3V3
- R81 pad 1: +3.3V -> +3V3
- R86 pad 1: +3.3V -> +3V3
- R88 pad 1: +3.3V -> +3V3
- R9 pad 1: +3.3V -> +3V3
- R93 pad 1: +3.3V -> +3V3
- R95 pad 1: +3.3V -> +3V3
- R98 pad 1: +3.3V -> +3V3
- R99 pad 1: +3.3V -> +3V3
- SW5 pad 5: +3.3V -> +3V3
- SW5 pad 6: +3.3V -> +3V3
- SW5 pad 7: +3.3V -> +3V3
- SW5 pad 8: +3.3V -> +3V3
- SW6 pad 5: +3.3V -> +3V3
- U1 pad 4: +3.3V -> +3V3
- U10 pad 2: +3.3V -> +3V3
- U11 pad 16: +3.3V -> +3V3
- U12 pad 5: +3.3V -> +3V3
- U12 pad 8: +3.3V -> +3V3
- U17 pad 2: +3.3V -> +3V3
- U2 pad 4: +3.3V -> +3V3
- U21 pad 2: +3.3V -> +3V3
- U23 pad 15: /actuators/line_led_pwm_3v3 -> /actuators/led_vbatt_error
- U23 pad 16: /actuators/led_vbatt_ok -> /actuators/led_vbatt_warning
- U23 pad 17: /actuators/led_vbatt_warning -> /actuators/led_vbatt_ok
- U23 pad 18: /actuators/led_vbatt_error -> /actuators/line_led_pwm_3v3
- U3 pad 1: +3.3V -> +3V3
- U31 pad 2: +3.3V -> +3V3
- U32 pad 2: +3.3V -> +3V3
- U35 pad 2: +3.3V -> +3V3
- U35 pad 4: +3.3V -> +3V3
- U4 pad 1: +3.3V -> +3V3
- U5 pad 5: +3.3V -> +3V3
- U6 pad 2: +3.3V -> +3V3
- U7 pad 16: +3.3V -> +3V3
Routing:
- net GND: track 59.0 -> 600.8 mm, vias 0 -> 23
- net +3V3: track 0.00 -> 333.8 mm, vias 0 -> 17
- net +5V: track 0.00 -> 192.3 mm, vias 0 -> 5
- net /actuators//reset_tof_3v3: track 0.00 -> 146.8 mm, vias 0 -> 5
- net /actuators/enable_tof_3v3: track 0.00 -> 146.8 mm, vias 0 -> 2
- net /com/sda_3v3: track 0.00 -> 137.8 mm, vias 0 -> 4
- net /com/scl_3v3: track 0.00 -> 132.7 mm, vias 0 -> 4
- net +BATT: track 0.00 -> 107.8 mm, vias 0 -> 4
- net /actuators/servo_pwm_0_3v3: track 0.00 -> 102.5 mm, vias 0 -> 2
- net /power_supply/enable_pw_conv_3v7: track 7.98 -> 104.6 mm, vias 0 -> 3
- net /sensors/enable_tof1: track 0.00 -> 95.4 mm
- net /sensors/tof_irq: track 0.00 -> 88.8 mm
- net /actuators/servo_pwm_1_3v3: track 0.00 -> 82.1 mm, vias 0 -> 2
- net /actuators/line_led_pwm_3v3: track 0.00 -> 73.5 mm, vias 0 -> 1
- net /actuators/LED_RGB_B_3v3: track 0.00 -> 69.6 mm, vias 0 -> 4
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
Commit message: pmi layout (WIP)
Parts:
- C47, C48, R10, R11, R12, R9, U7: moved to B.Cu
- moved C12 341.2 mm to (-41.0, 279.7)
- moved C31 341.2 mm to (-58.5, 245.5)
- moved C32 341.2 mm to (-40.2, 227.0)
- moved C33 341.2 mm to (-8.75, 225.5)
- moved C34 341.2 mm to (-35.0, 225.5)
- moved C35 341.2 mm to (-37.0, 225.3)
- moved C49 341.2 mm to (28.0, 256.0)
- moved C50 341.2 mm to (27.8, 258.7)
- moved D4 341.2 mm to (-60.7, 205.8)
- moved D5 341.2 mm to (-60.7, 201.3)
- moved D6 341.2 mm to (-7.00, 226.8)
- moved J6 341.2 mm to (10.6, 226.9)
- moved J7 341.2 mm to (-48.0, 223.7)
- moved Q2 341.2 mm to (-59.0, 230.0)
- moved R100 341.2 mm to (-9.45, 236.3)
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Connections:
- U7 pad 14: /sensors/scl_3v3 -> /com/scl_3v3
- U7 pad 15: /sensors/sda_3v3 -> /com/sda_3v3
- U7 pad 4: /line_detect_l0 -> /line_detect_l2
- U7 pad 6: /line_detect_l2 -> /line_detect_l3
- U7 pad 7: /line_detect_l3 -> /line_detect_l0
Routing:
- net +3V3: track 333.8 -> 449.6 mm, vias 17 -> 26
- net GND: track 600.8 -> 690.4 mm, vias 23 -> 32
- net /propulsion/pwm_vaccum_3v3: track 27.9 -> 101.4 mm, vias 2 -> 4
- net /line_detect_l3: track 0.00 -> 68.5 mm
- net /line_detect_l2: track 0.00 -> 64.0 mm, vias 0 -> 4
- net /line_detect_l1: track 1.49 -> 58.1 mm, vias 0 -> 2
- net /line_detect_l0: track 1.49 -> 55.8 mm
- net /line_detect_r0: track 1.49 -> 51.5 mm
- net /line_detect_r1: track 1.49 -> 43.3 mm
- net +BATT: track 107.8 -> 142.9 mm, vias 4 -> 5
- net /line_detect_r2: track 1.51 -> 35.7 mm
- net /line_detect_r3: track 1.49 -> 23.9 mm
- net /com/scl_3v3: track 132.7 -> 152.1 mm, vias 4 -> 7
- net /com/sda_3v3: track 137.8 -> 155.7 mm, vias 4 -> 7
- net /sensors/i2C_io_int_3v3: track 0.00 -> 5.87 mm
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
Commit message: pmi layout (WIP)
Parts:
- moved C12 158.9 mm to (117.9, 275.3)
- moved C31 158.9 mm to (100.4, 241.2)
- moved C32 158.9 mm to (118.6, 222.7)
- moved C33 158.9 mm to (150.1, 221.2)
- moved C34 158.9 mm to (123.9, 221.2)
- moved C35 158.9 mm to (121.9, 220.9)
- moved C49 158.9 mm to (186.8, 251.6)
- moved C50 158.9 mm to (186.6, 254.4)
- moved D4 158.9 mm to (98.1, 201.4)
- moved D5 158.9 mm to (98.1, 196.9)
- moved D6 158.9 mm to (151.8, 222.4)
- moved J6 158.9 mm to (169.4, 222.6)
- moved J7 158.9 mm to (110.9, 219.3)
- moved Q2 158.9 mm to (99.9, 225.7)
- moved R100 158.9 mm to (149.4, 231.9)
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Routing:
- net /sensors/tof_irq: track 92.1 -> 148.7 mm, vias 0 -> 1
- net /com/vbatt_mon_4.35V: track 0.00 -> 52.9 mm, vias 0 -> 3
- net /com/scl_3v3: track 152.1 -> 185.6 mm, vias 7 -> 8
- net /com/sda_3v3: track 155.7 -> 188.6 mm, vias 7 -> 8
- net +3V3: track 449.6 -> 434.8 mm, vias 26 -> 28
- net /sensors/ctc_left: track 0.00 -> 14.2 mm, vias 0 -> 1
- net /sensors/ctc_rigth: track 0.00 -> 11.8 mm, vias 0 -> 1
- net /propulsion/left_encod_B_3v3: track 2.75 -> 14.4 mm, vias 0 -> 1
- net +5V: track 192.3 -> 181.4 mm, vias 5 -> 7
- net /propulsion/right_encod_A_3v3: track 2.75 -> 13.0 mm, vias 0 -> 1
- net /propulsion/left_encod_A_3v3: track 2.77 -> 12.8 mm, vias 0 -> 1
- net /propulsion/right_encod_B_3v3: track 2.76 -> 11.1 mm, vias 0 -> 1
- net /com/i_prop_left_3v3: track 4.17 -> 10.4 mm
- net GND: track 690.4 -> 696.2 mm
- net /propulsion/pwm_right: track 3.05 -> 8.15 mm
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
